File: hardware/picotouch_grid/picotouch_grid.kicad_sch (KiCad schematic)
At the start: 172 parts, among them J1 TRRS, J2 TRRS, J3 TRRS, U1 Pico, U2 TS20, U3 TS20, U5 H11L1

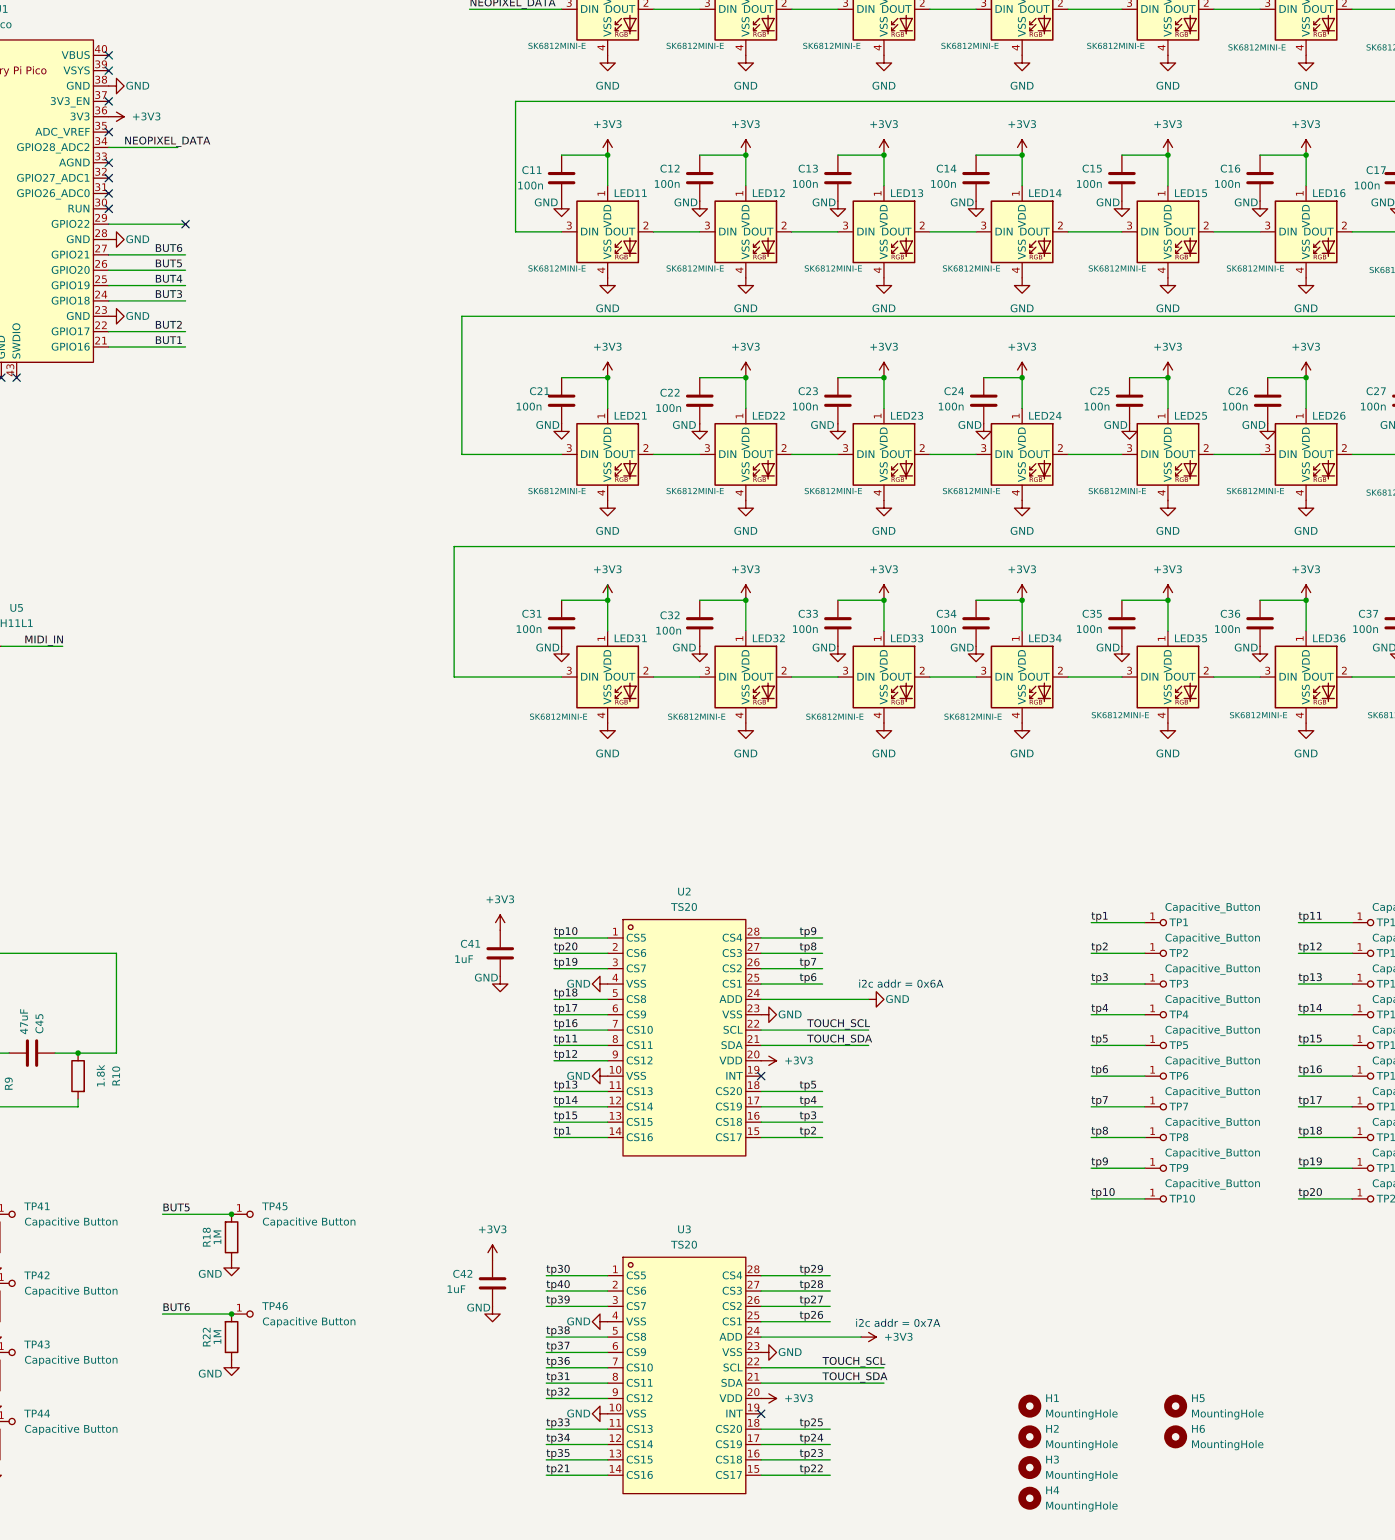
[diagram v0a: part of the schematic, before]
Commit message: getting back into this, updated some stuff, getting lots of ERC, got some power pins wrong?
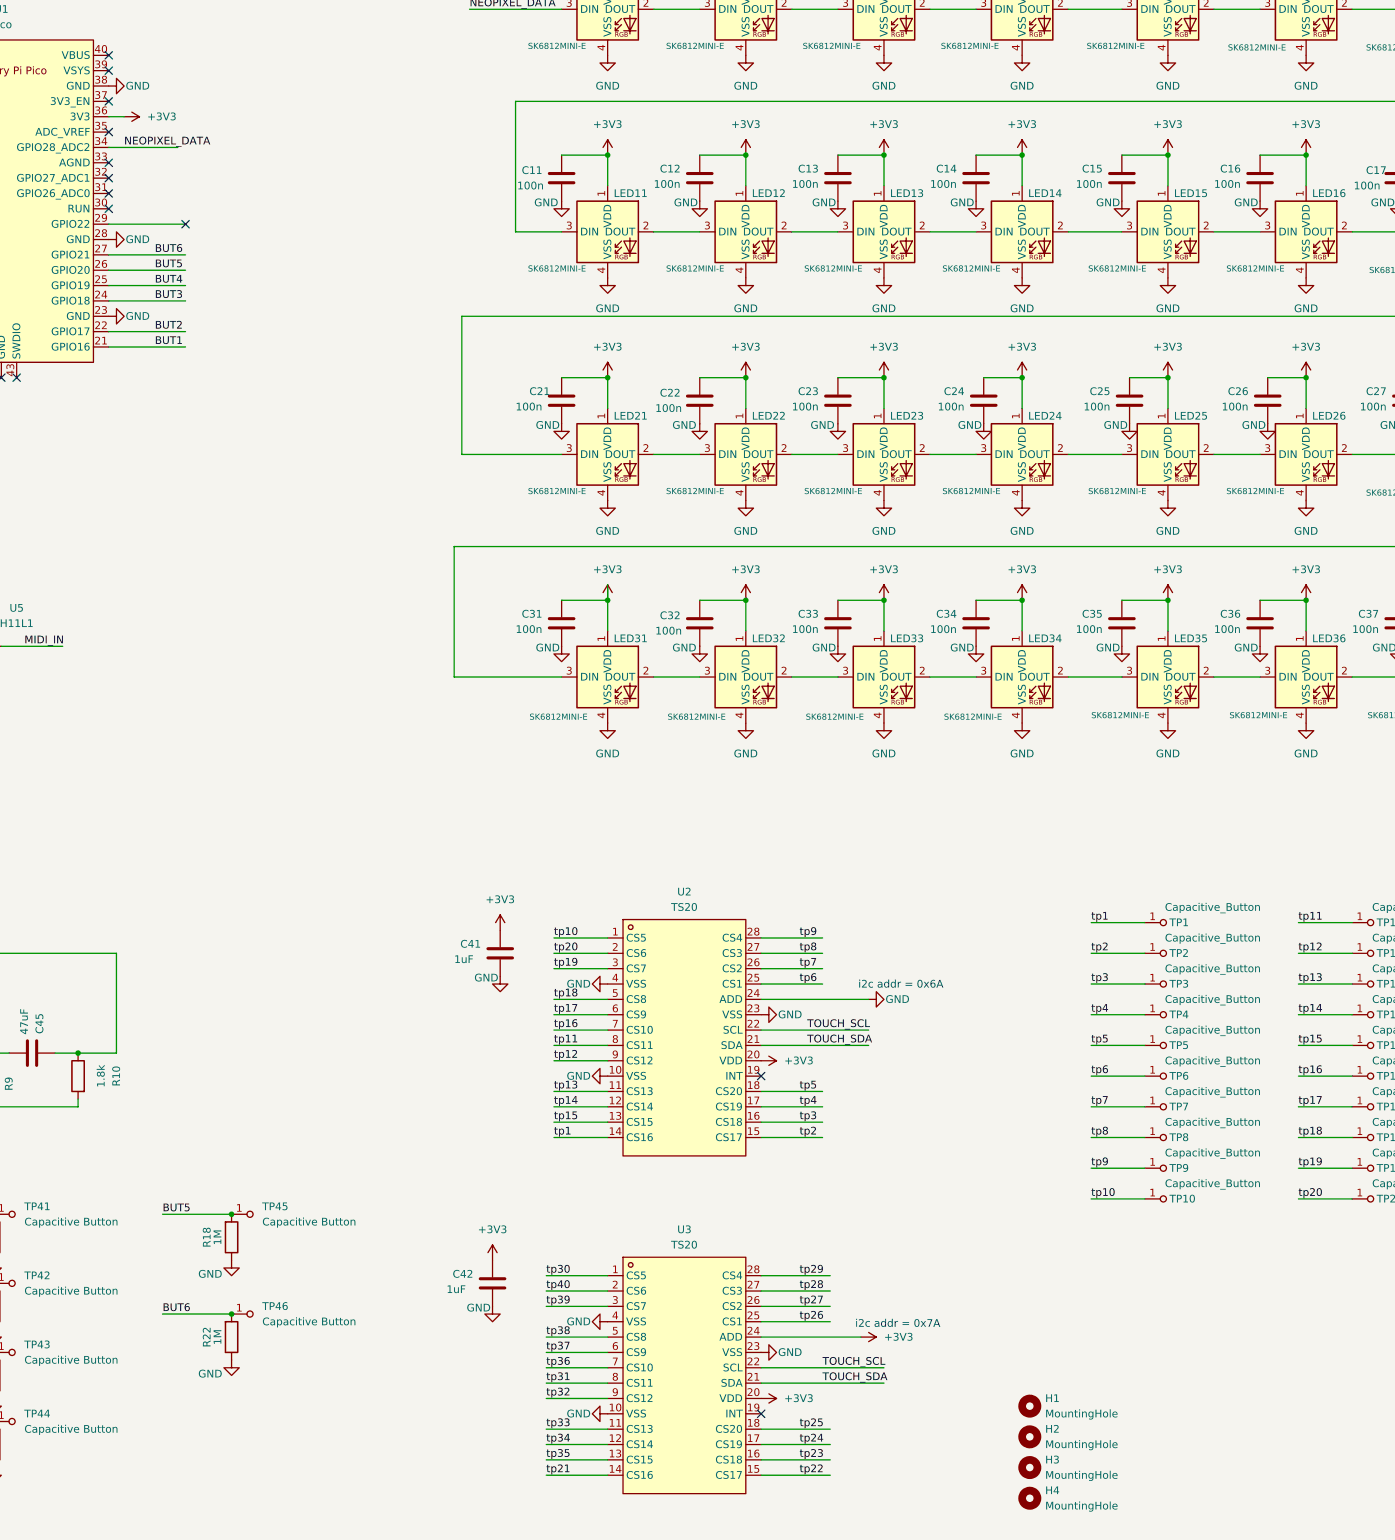
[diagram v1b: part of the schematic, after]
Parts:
- removed H5, H6: MountingHole, MountingHole:MountingHole_2.1mm, symbol Mechanical:MountingHole
- DISP1: footprint todbot_stuff:OLED-TH_under_L27.8-W27.2-P2.54_C9900033791 -> easyeda2kicad:OLED-TH_L27.8-W27.2-P2.54_C9900033791
- TP45, TP46: footprint todbot_stuff:Pad-CapacitiveTouch-SparkFun-10x5mm-roundrect -> SparkFun-Switch:Pad-CapacitiveTouch
- U1: footprint todbot_RPI_Pico:RPi_Pico_SMD -> RPi_Pico:RPi_Pico_SMD_TH
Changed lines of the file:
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@@
 	(wire
 		(pts
+			(xy 106.68 49.53) (xy 104.14 49.53)
+		)
+		(stroke
+			(width 0)
+			(type default)
+		)
+	)
+	(wire
+		(pts
 			(xy 44.45 187.96) (xy 52.07 187.96)
 		)
@@
 			)
 		)
-		(property "Footprint" "todbot_stuff:OLED-TH_under_L27.8-W27.2-P2.54_C9900033791"
+		(property "Footprint" "easyeda2kicad:OLED-TH_L27.8-W27.2-P2.54_C9900033791"
 			(at 34.29 91.44 0)
 			(effects
@@
 			)
 		)
-		(property "Footprint" "todbot_RPI_Pico:RPi_Pico_SMD"
+		(property "Footprint" "RPi_Pico:RPi_Pico_SMD_TH"
 			(at 86.36 63.5 90)
 			(effects
@@
 			)
 		)
-		(property "Footprint" "todbot_stuff:Pad-CapacitiveTouch-SparkFun-10x5mm-roundrect"
+		(property "Footprint" "SparkFun-Switch:Pad-CapacitiveTouch"
 			(at 116.84 247.65 0)
 			(effects
@@
 	)
 	(symbol
-		(lib_id "Mechanical:MountingHole")
-		(at 280.67 262.89 0)
-		(unit 1)
-		(exclude_from_sim yes)
-		(in_bom no)
-		(on_board yes)
-		(dnp no)
-		(fields_autoplaced yes)
-		(property "Reference" "H5"
-			(at 283.21 261.6199 0)
-			(effects
-				(font
-					(size 1.27 1.27)
-				)
-				(justify left)
-			)
-		)
-		(property "Value" "MountingHole"
-			(at 283.21 264.1599 0)
-			(effects
-				(font
-					(size 1.27 1.27)
-				)
-				(justify left)
-			)
-		)
-		(property "Footprint" "MountingHole:MountingHole_2.1mm"
-			(at 280.67 262.89 0)
-			(effects
-				(font
-					(size 1.27 1.27)
-				)
-				(hide yes)
-			)
-		)
-		(property "Datasheet" "~"
-			(at 280.67 262.89 0)
-			(effects
-				(font
-					(size 1.27 1.27)
-				)
-				(hide yes)
-			)
-		)
-		(property "Description" "Mounting Hole without connection"
-			(at 280.67 262.89 0)
-			(effects
-				(font
-					(size 1.27 1.27)
-				)
-				(hide yes)
-			)
-		)
-		(instances
-			(project "picotouch_grid"
-				(path "/036e8f10-ba17-4cdc-95e8-e722ded3fffe"
-					(reference "H5")
-					(unit 1)
-				)
-			)
-		)
-	)
-	(symbol
 		(lib_id "PCM_marbastlib-various:SK6812MINI-E")
 		(at 302.26 68.58 0)
@@
 	(symbol
 		(lib_id "power:+3V3")
-		(at 104.14 49.53 270)
+		(at 106.68 49.53 270)
 		(unit 1)
 		(exclude_from_sim no)
@@
 		(fields_autoplaced yes)
 		(property "Reference" "#PWR089"
-			(at 100.33 49.53 0)
+			(at 102.87 49.53 0)
 			(effects
 				(font
@@
 		)
 		(property "Value" "+3V3"
-			(at 107.95 49.5299 90)
+			(at 110.49 49.5299 90)
 			(effects
 				(font
@@
 		)
 		(property "Footprint" ""
-			(at 104.14 49.53 0)
+			(at 106.68 49.53 0)
 			(effects
 				(font
@@
 		)
 		(property "Datasheet" ""
-			(at 104.14 49.53 0)
+			(at 106.68 49.53 0)
 			(effects
 				(font
@@
 		)
 		(property "Description" "Power symbol creates a global label with name \"+3V3\""
-			(at 104.14 49.53 0)
+			(at 106.68 49.53 0)
 			(effects
 				(font
@@
 	)
 	(symbol
-		(lib_id "Mechanical:MountingHole")
-		(at 280.67 267.97 0)
-		(unit 1)
-		(exclude_from_sim yes)
-		(in_bom no)
-		(on_board yes)
-		(dnp no)
-		(fields_autoplaced yes)
-		(property "Reference" "H6"
-			(at 283.21 266.6999 0)
-			(effects
-				(font
-					(size 1.27 1.27)
-				)
-				(justify left)
-			)
-		)
-		(property "Value" "MountingHole"
-			(at 283.21 269.2399 0)
-			(effects
-				(font
-					(size 1.27 1.27)
-				)
-				(justify left)
-			)
-		)
-		(property "Footprint" "MountingHole:MountingHole_2.1mm"
-			(at 280.67 267.97 0)
-			(effects
-				(font
-					(size 1.27 1.27)
-				)
-				(hide yes)
-			)
-		)
-		(property "Datasheet" "~"
-			(at 280.67 267.97 0)
-			(effects
-				(font
-					(size 1.27 1.27)
-				)
-				(hide yes)
-			)
-		)
-		(property "Description" "Mounting Hole without connection"
-			(at 280.67 267.97 0)
-			(effects
-				(font
-					(size 1.27 1.27)
-				)
-				(hide yes)
-			)
-		)
-		(instances
-			(project "picotouch_grid"
-				(path "/036e8f10-ba17-4cdc-95e8-e722ded3fffe"
-					(reference "H6")
-					(unit 1)
-				)
-			)
-		)
-	)
-	(symbol
 		(lib_id "SparkFun-Switch:Capacitive Button")
 		(at 124.46 231.14 270)
@@
 			)
 		)
-		(property "Footprint" "todbot_stuff:Pad-CapacitiveTouch-SparkFun-10x5mm-roundrect"
+		(property "Footprint" "SparkFun-Switch:Pad-CapacitiveTouch"
 			(at 116.84 231.14 0)
 			(effects
